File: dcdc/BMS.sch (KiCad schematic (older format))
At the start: 49 parts, among them J1 MM3474, J2 Conn_01x01, J3 Conn_01x01, J4 Conn_01x01, J5 Conn_01x01, J6 Conn_01x05, Q1 BSS138, Q2 IRF7403, Q3 IRF7403, Q4 BSS138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

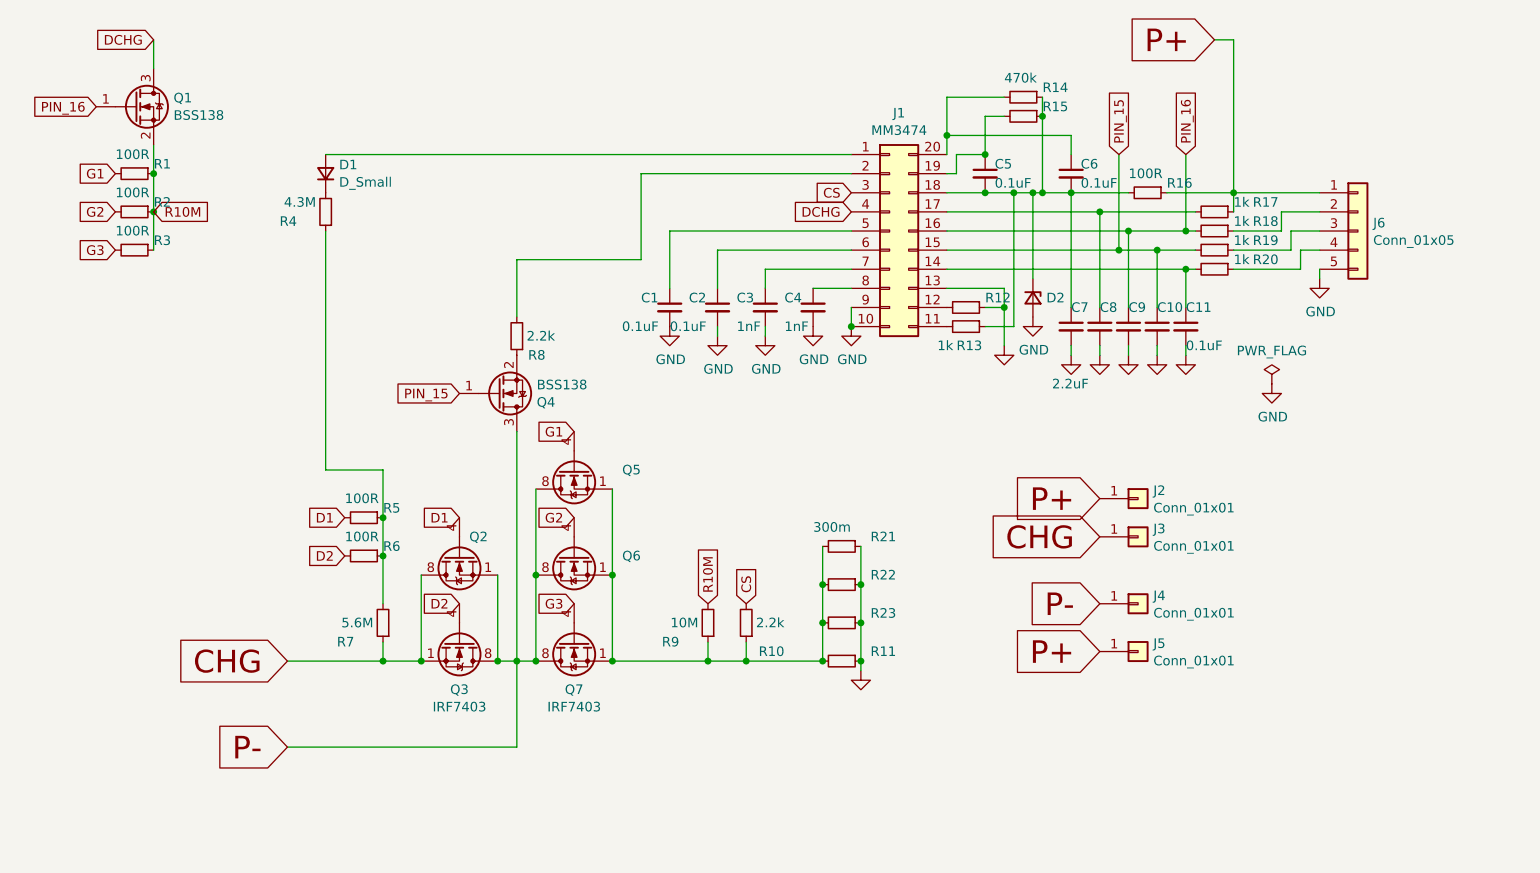
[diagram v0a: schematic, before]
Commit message: update schematic
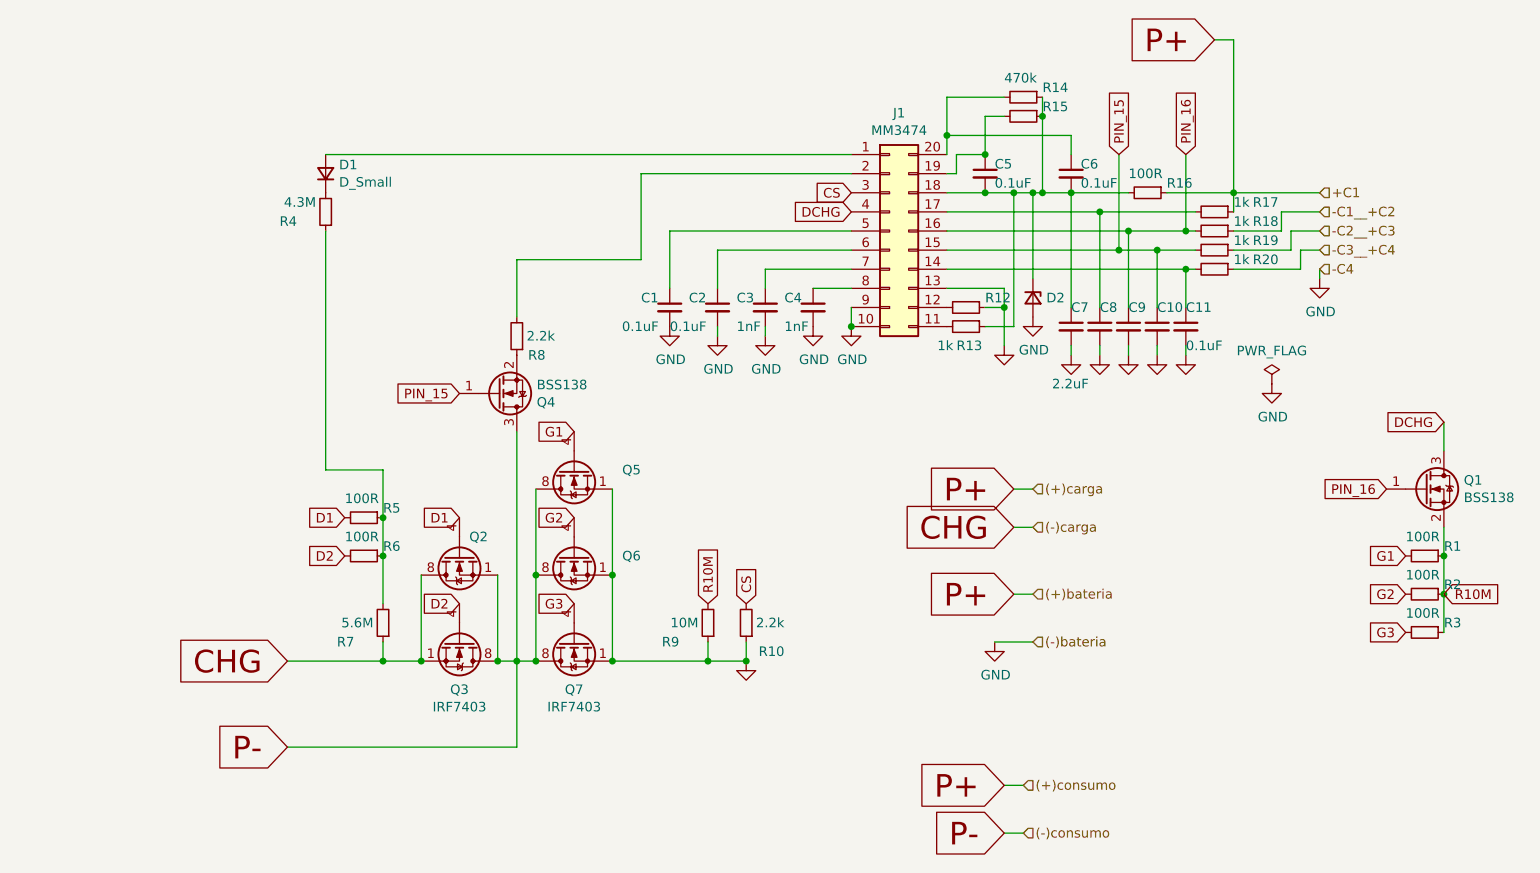
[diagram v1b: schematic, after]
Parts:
- removed J2, J3, J4, J5: Conn_01x01, symbol Connector_Generic:Conn_01x01
- removed J6: Conn_01x05, symbol Connector_Generic:Conn_01x05
- removed R11, R21, R22, R23: 300m, Resistor_SMD:R_2512_6332Metric_Pad1.52x3.35mm_HandSolder, symbol Device:R_Small
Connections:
- net GND: now also Q5.1 (S), Q5.2 (S), Q5.3 (S), Q6.1 (S), Q6.2 (S), Q6.3 (S), Q7.1 (S), Q7.2 (S), Q7.3 (S), R10.1, R9.1
- net -C3__+C4: now reaches R20.1
- net -C2__+C3: now reaches R19.1
- net -C1__+C2: now reaches R18.1
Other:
- moved on the sheet: Q1, R1, R2, R3

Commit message: first end
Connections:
- net CHG: now also Q2.1 (S), Q2.2 (S), Q2.3 (S); no longer Q2.5 (D), Q2.6 (D), Q2.7 (D), Q2.8 (D)
- net P-: now also Q2.5 (D), Q2.6 (D), Q2.7 (D), Q2.8 (D); no longer Q2.1 (S), Q2.2 (S), Q2.3 (S)
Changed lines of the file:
@@
 Text GLabel 6150 2550 0    50   Input ~ 0
 CS
-$Comp
-L Transistor_FET:IRF7403 Q?
-U 1 1 61770BEE
-P 4100 4900
-AR Path="/61770BEE" Ref="Q?"  Part="1"
-AR Path="/6175823F/61770BEE" Ref="Q3"  Part="1"
-F 0 "Q3" V 4349 4900 50  0000 C CNN
-F 1 "IRF7403" V 4440 4900 50  0000 C CNN
-F 2 "Package_SO:SOIC-8_3.9x4.9mm_P1.27mm" H 4300 4800 50  0001 L CNN
-F 3 "https://www.infineon.com/dgdl/irf7403pbf.pdf?fileId=5546d462533600a4015355fa23541b9c" H 4100 4900 50  0001 L CNN
-	1    4100 4900
-	0    1    1    0
-$EndComp
 Connection ~ 4900 5000
 $Comp
@@
 F 3 "https://www.infineon.com/dgdl/irf7403pbf.pdf?fileId=5546d462533600a4015355fa23541b9c" H 4100 4450 50  0001 L CNN
 	1    4100 4450
-	0    -1   1    0
+	0    1    1    0
 $EndComp
 Wire Wire Line
@@
 	1    0    0    -1
 $EndComp
+Connection ~ 6150 3250
+$Comp
+L Connector_Generic:Conn_02x10_Counter_Clockwise J?
+U 1 1 61770ADF
+P 6350 2750
+AR Path="/61770ADF" Ref="J?"  Part="1"
+AR Path="/6175823F/61770ADF" Ref="J1"  Part="1"
+F 0 "J1" H 6400 3367 50  0000 C CNN
+F 1 "MM3474" H 6400 3276 50  0000 C CNN
+F 2 "Package_SO:SSOP-20_4.4x6.5mm_P0.65mm" H 6350 2750 50  0001 C CNN
+F 3 "~" H 6350 2750 50  0001 C CNN
+	1    6350 2750
+	1    0    0    -1
+$EndComp
+$Comp
+L power:GND #PWR?
+U 1 1 61B581D4
+P 6900 4900
+AR Path="/61B581D4" Ref="#PWR?"  Part="1"
+AR Path="/6175823F/61B581D4" Ref="#PWR0117"  Part="1"
+F 0 "#PWR0117" H 6900 4650 50  0001 C CNN
+F 1 "GND" H 6905 4727 50  0000 C CNN
+F 2 "" H 6900 4900 50  0001 C CNN
+F 3 "" H 6900 4900 50  0001 C CNN
+	1    6900 4900
+	1    0    0    -1
+$EndComp
+Text GLabel 7000 4650 0    118  Input ~ 0
+P+
+Text GLabel 6950 5650 0    118  Input ~ 0
+P+
+Text GLabel 6950 5900 0    118  Input ~ 0
+P-
+Text HLabel 7050 5650 2    50   Input ~ 0
+(+)consumo
+Text HLabel 7050 5900 2    50   Input ~ 0
+(-)consumo
+Wire Wire Line
+	7050 5650 6950 5650
+Wire Wire Line
+	6950 5900 7050 5900
+Text HLabel 7100 4100 2    50   Input ~ 0
+(+)carga
+Text HLabel 7100 4300 2    50   Input ~ 0
+(-)carga
+Text HLabel 7100 4650 2    50   Input ~ 0
+(+)bateria
+Text HLabel 7100 4900 2    50   Input ~ 0
+(-)bateria
+Wire Wire Line
+	7100 4100 7000 4100
+Wire Wire Line
+	7000 4300 7100 4300
+Wire Wire Line
+	7100 4650 7000 4650
+Wire Wire Line
+	6900 4900 7100 4900
+Text HLabel 8600 2550 2    50   Input ~ 0
++C1
+Text HLabel 8600 2650 2    50   Input ~ 0
+-C1__+C2
+Text HLabel 8600 2750 2    50   Input ~ 0
+-C2__+C3
+Text HLabel 8600 2850 2    50   Input ~ 0
+-C3__+C4
+Text HLabel 8600 2950 2    50   Input ~ 0
+-C4
+$Comp
+L Transistor_FET:IRF7403 Q?
+U 1 1 61770BEE
+P 4100 4900
+AR Path="/61770BEE" Ref="Q?"  Part="1"
+AR Path="/6175823F/61770BEE" Ref="Q3"  Part="1"
+F 0 "Q3" V 4349 4900 50  0000 C CNN
+F 1 "IRF7403" V 4440 4900 50  0000 C CNN
+F 2 "Package_SO:SOIC-8_3.9x4.9mm_P1.27mm" H 4300 4800 50  0001 L CNN
+F 3 "https://www.infineon.com/dgdl/irf7403pbf.pdf?fileId=5546d462533600a4015355fa23541b9c" H 4100 4900 50  0001 L CNN
+	1    4100 4900
+	0    1    1    0
+$EndComp
 $Comp
 L Transistor_FET:BSS138 Q?
@@
 	1    0    0    1
 $EndComp
-Connection ~ 6150 3250
-$Comp
-L Connector_Generic:Conn_02x10_Counter_Clockwise J?
-U 1 1 61770ADF
-P 6350 2750
-AR Path="/61770ADF" Ref="J?"  Part="1"
-AR Path="/6175823F/61770ADF" Ref="J1"  Part="1"
-F 0 "J1" H 6400 3367 50  0000 C CNN
-F 1 "MM3474" H 6400 3276 50  0000 C CNN
-F 2 "Package_SO:SSOP-20_4.4x6.5mm_P0.65mm" H 6350 2750 50  0001 C CNN
-F 3 "~" H 6350 2750 50  0001 C CNN
-	1    6350 2750
-	1    0    0    -1
-$EndComp
-$Comp
-L power:GND #PWR?
-U 1 1 61B581D4
-P 6900 4900
-AR Path="/61B581D4" Ref="#PWR?"  Part="1"
-AR Path="/6175823F/61B581D4" Ref="#PWR0117"  Part="1"
-F 0 "#PWR0117" H 6900 4650 50  0001 C CNN
-F 1 "GND" H 6905 4727 50  0000 C CNN
-F 2 "" H 6900 4900 50  0001 C CNN
-F 3 "" H 6900 4900 50  0001 C CNN
-	1    6900 4900
-	1    0    0    -1
-$EndComp
-Text GLabel 7000 4650 0    118  Input ~ 0
-P+
-Text GLabel 6950 5650 0    118  Input ~ 0
-P+
-Text GLabel 6950 5900 0    118  Input ~ 0
-P-
-Text HLabel 7050 5650 2    50   Input ~ 0
-(+)consumo
-Text HLabel 7050 5900 2    50   Input ~ 0
-(-)consumo
-Wire Wire Line
-	7050 5650 6950 5650
-Wire Wire Line
-	6950 5900 7050 5900
-Text HLabel 7100 4100 2    50   Input ~ 0
-(+)carga
-Text HLabel 7100 4300 2    50   Input ~ 0
-(-)carga
-Text HLabel 7100 4650 2    50   Input ~ 0
-(+)bateria
-Text HLabel 7100 4900 2    50   Input ~ 0
-(-)bateria
-Wire Wire Line
-	7100 4100 7000 4100
-Wire Wire Line
-	7000 4300 7100 4300
-Wire Wire Line
-	7100 4650 7000 4650
-Wire Wire Line
-	6900 4900 7100 4900
-Text HLabel 8600 2550 2    50   Input ~ 0
-+C1
-Text HLabel 8600 2650 2    50   Input ~ 0
--C1__+C2
-Text HLabel 8600 2750 2    50   Input ~ 0
--C2__+C3
-Text HLabel 8600 2850 2    50   Input ~ 0
--C3__+C4
-Text HLabel 8600 2950 2    50   Input ~ 0
--C4
 $EndSCHEMATC
